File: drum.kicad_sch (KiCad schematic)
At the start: 39 parts, among them J101 CORTEX-DEBUG, J102 JAE_DX07S016JA3, SW101 SW_Push, SW102 SW_Push, U101 ATSAMD51J, U102 TPS78433QWDRBRQ1, Y101 32k768

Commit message: Update parts
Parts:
- C101: footprint Capacitor_SMD:C_0603_1608Metric -> V2_Capacitor_SMD:C_0603; symbol Device:C_Small -> V2_Device:C_0603_10u; Manufacturer (none) -> TDK; Mouser (none) -> 810-C1608X6S1A106M; Product (none) -> C1608X6S1A106M080AC
- C102, C103, C104, C105, C106: footprint Capacitor_SMD:C_0603_1608Metric -> V2_Capacitor_SMD:C_0603; symbol Device:C_Small -> V2_Device:C_0603_0u1; Manufacturer (none) -> TDK; Mouser (none) -> 810-CGA3E2X7R1H104MA; Product (none) -> CGA3E2X7R1H104M080AA
- C107, C108: footprint Capacitor_SMD:C_0603_1608Metric -> V2_Capacitor_SMD:C_0603; symbol Device:C_Small -> V2_Device:C_0603_18p; Manufacturer (none) -> YAGEO; Mouser (none) -> 603-CC603JRNPO9BN180; Product (none) -> CC0603JRNPO9BN180
- C109, C110: footprint Capacitor_SMD:C_0805_2012Metric -> V2_Capacitor_SMD:C_0805; symbol Device:C_Small -> V2_Device:C_0805_10u; Manufacturer (none) -> TDK; Mouser (none) -> 810-C2012X5R1E106K; Product (none) -> C2012X5R1E106K125AB; Rating (none) -> 25V
- D101: footprint LED_SMD:LED_0603_1608Metric -> V2_LED:LED_0603; symbol Device:LED_Small -> V2_Device:LED_0603_Orange; Manufacturer (none) -> ROHM Semiconductor; Mouser (none) -> 755-SML-D12M8WT86C; Product (none) -> SML-D12M8WT86C
- D102, D103: LCSC (none) -> C965555; Manufacturer (none) -> Worldsemi; Product (none) -> WS2812B-2020
- ESD101: Manufacturer (none) -> Semtech; Mouser (none) -> 947-RCLAMP0582N.TCT; Product (none) -> RCLAMP0582N.TCT
- FID101, FID102, FID103: value Fiducial -> Fiducial_Paste
- INFO102: value ORDER-NUMBER -> Order_Number
- J101: value CORTEX-DEBUG -> Cortex_Debug
- J102: value JAE_DX07S016JA3 -> DX07S016JA3; Manufacturer (none) -> JAE Electronics; Mouser (none) -> 656-DX07S016JA3R1500; Product (none) -> DX07S016JA3R1500
- R101: footprint Resistor_SMD:R_0603_1608Metric -> V2_Resistor_SMD:R_0603; symbol Device:R_Small -> V2_Device:R_0603_330R; Manufacturer (none) -> Vishay; Mouser (none) -> 71-CRCW0603330RFKEAC; Product (none) -> CRCW0603330RFKEAC; Rating (none) -> 100mW
- R102, R103: footprint Resistor_SMD:R_0603_1608Metric -> V2_Resistor_SMD:R_0603; symbol Device:R_Small -> V2_Device:R_0603_5k1; Manufacturer (none) -> Vishay; Mouser (none) -> 71-CRCW06035K10FKEAC; Product (none) -> CRCW06035K10FKEAC; Rating (none) -> 100mW
- R104: footprint Resistor_SMD:R_0603_1608Metric -> V2_Resistor_SMD:R_0603; symbol Device:R_Small -> V2_Device:R_0603_100k; Manufacturer (none) -> Vishay; Mouser (none) -> 71-CRCW0603100KFKEAC; Product (none) -> CRCW0603100KFKEAC; Rating (none) -> 100mW
- SW101, SW102: value SW_Push -> SKSG; symbol Switch:SW_Push -> V2_Switch:SKSG; Manufacturer (none) -> Alps Alpine; Mouser (none) -> 688-SKSGACE010; Product (none) -> SKSGACE010
- TVS101: value SMAJ36CA -> SMBJ36CA; footprint Diode_SMD:D_SMA -> V2_Diode_SMD:D_SMB; symbol V2_Diode:SMAJ36CA -> V2_Diode:SMBJ36CA; Manufacturer (none) -> Bourns; Mouser (none) -> 652-SMBJ36CA-Q; Product (none) -> SMBJ36CA-Q; Rating (none) -> 36V
- U101: Manufacturer (none) -> Microchip Technology; Mouser (none) -> 556-ATSAMD51J19AMU; Product (none) -> ATSAMD51J19A-MU
- U102: Manufacturer (none) -> Texas Instruments; Mouser (none) -> 595-TPS78433QWDRBRQ1; Product (none) -> TPS78433QWDRBRQ1
- Y101: symbol Device:Crystal_Small -> V2_Device:Crystal_3.2x1.5_32k768; Manufacturer (none) -> ABRACON; Mouser (none) -> 815-ABS0716632.768KT; Product (none) -> ABS07-166-32.768KHZ-T
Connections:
- net USB-Shield renamed Shield
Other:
- moved on the sheet: FID101, FID102, FID103, INFO102

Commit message: Update library
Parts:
- C101: Rating (none) -> 10V
- C102, C103, C104, C105, C106: Rating (none) -> 50V
- D101: Mouser 755-SML-D12M8WT86C -> 755-SML-D12D1WT86; Product SML-D12M8WT86C -> SML-D12D1WT86
- TVS101: value SMBJ36CA -> SMBJ33CA; symbol V2_Diode:SMBJ36CA -> V2_Diode:SMBJ33CA; Mouser 652-SMBJ36CA-Q -> 652-SMBJ33CA-Q; Product SMBJ36CA-Q -> SMBJ33CA-Q; Rating 36V -> 33V
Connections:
- net +24V-Supply renamed +VLINK
- net VBUS renamed +VBUS
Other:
- note added: "Power +28V"
- note removed: "Power +24V"
- moved on the sheet: TVS101

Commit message: Update library
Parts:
- J101: value Cortex_Debug -> Cortex; footprint V2_Cortex_Debug:Cortex_Debug_Pad -> V2_Connector_Debug:Cortex; symbol V2_Cortex_Debug:Cortex_Debug -> V2_Connector_Debug:Cortex
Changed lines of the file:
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@@
 		(at 240.03 170.18 0)
 		(unit 1)
-		(exclude_from_sim yes)
+		(exclude_from_sim no)
 		(in_bom no)
 		(on_board yes)
@@
 			)
 		)
+		(property "Sim.Enable" "0"
+			(at 240.03 170.18 0)
+			(effects
+				(font
+					(size 1.27 1.27)
+				)
+				(hide yes)
+			)
+		)
 		(instances
 			(project ""
@@
 		(at 227.33 180.34 0)
 		(unit 1)
-		(exclude_from_sim yes)
+		(exclude_from_sim no)
 		(in_bom no)
 		(on_board yes)
@@
 			)
 		)
+		(property "Sim.Enable" "0"
+			(at 227.33 180.34 0)
+			(effects
+				(font
+					(size 1.27 1.27)
+				)
+				(hide yes)
+			)
+		)
 		(instances
 			(project "pulse"
@@
 		(at 157.48 190.5 270)
 		(unit 1)
-		(exclude_from_sim yes)
+		(exclude_from_sim no)
 		(in_bom no)
 		(on_board yes)
@@
 			)
 		)
+		(property "Sim.Enable" "0"
+			(at 157.48 190.5 0)
+			(effects
+				(font
+					(size 1.27 1.27)
+				)
+				(hide yes)
+			)
+		)
 		(instances
 			(project "hihat-1"
@@
 	)
 	(symbol
-		(lib_id "V2_Cortex_Debug:Cortex_Debug")
+		(lib_id "V2_Connector_Debug:Cortex")
 		(at 124.46 107.95 0)
 		(unit 1)
@@
 			)
 		)
-		(property "Value" "Cortex_Debug"
+		(property "Value" "Cortex"
 			(at 125.73 97.79 0)
 			(effects
@@
 			)
 		)
-		(property "Footprint" "V2_Cortex_Debug:Cortex_Debug_Pad"
+		(property "Footprint" "V2_Connector_Debug:Cortex"
 			(at 124.46 121.92 0)
 			(effects
@@
 		(at 240.03 165.1 0)
 		(unit 1)
-		(exclude_from_sim yes)
+		(exclude_from_sim no)
 		(in_bom no)
 		(on_board yes)
@@
 			)
 		)
+		(property "Sim.Enable" "0"
+			(at 240.03 165.1 0)
+			(effects
+				(font
+					(size 1.27 1.27)
+				)
+				(hide yes)
+			)
+		)
 		(instances
 			(project ""
@@
 		(at 157.48 184.15 270)
 		(unit 1)
-		(exclude_from_sim yes)
+		(exclude_from_sim no)
 		(in_bom no)
 		(on_board yes)
@@
 			)
 		)
+		(property "Sim.Enable" "0"
+			(at 157.48 184.15 0)
+			(effects
+				(font
+					(size 1.27 1.27)
+				)
+				(hide yes)
+			)
+		)
 		(instances
 			(project "hihat-1"
@@
 		(at 157.48 177.8 270)
 		(unit 1)
-		(exclude_from_sim yes)
+		(exclude_from_sim no)
 		(in_bom no)
 		(on_board yes)
@@
 			)
 		)
+		(property "Sim.Enable" "0"
+			(at 157.48 177.8 0)
+			(effects
+				(font
+					(size 1.27 1.27)
+				)
+				(hide yes)
+			)
+		)
 		(instances
 			(project "hihat-1"
@@
 		(at 157.48 171.45 270)
 		(unit 1)
-		(exclude_from_sim yes)
+		(exclude_from_sim no)
 		(in_bom no)
 		(on_board yes)
@@
 			)
 		)
+		(property "Sim.Enable" "0"
+			(at 157.48 171.45 0)
+			(effects
+				(font
+					(size 1.27 1.27)
+				)
+				(hide yes)
+			)
+		)
 		(instances
 			(project ""
@@
 		(at 212.09 167.64 0)
 		(unit 1)
-		(exclude_from_sim yes)
+		(exclude_from_sim no)
 		(in_bom no)
 		(on_board yes)
@@
 			(at 212.09 167.64 0)
 			(effects
+				(font
+					(size 1.27 1.27)
+				)
+				(hide yes)
+			)
+		)
+		(property "Sim.Enable" "0"
+			(at 212.09 167.64 0)
+			(effects

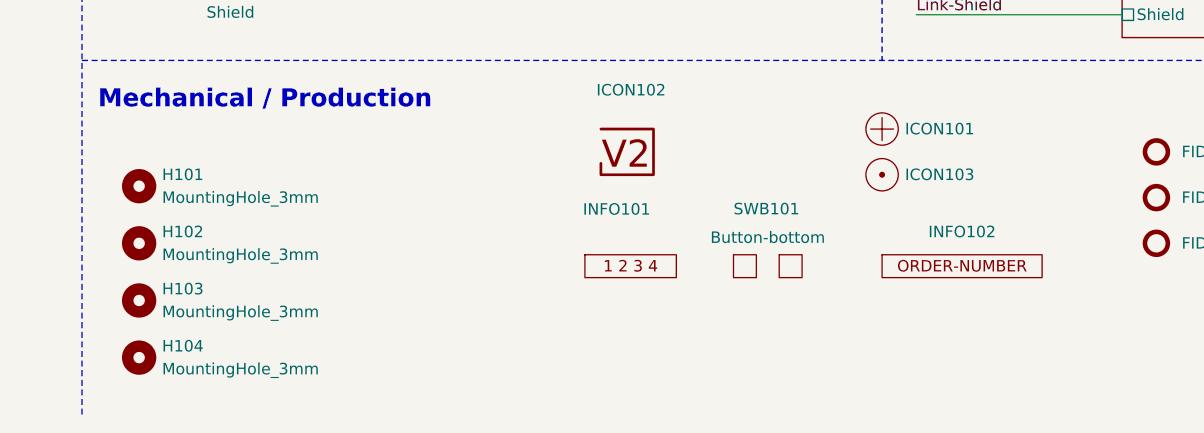
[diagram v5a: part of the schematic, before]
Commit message: Replace Order_Number
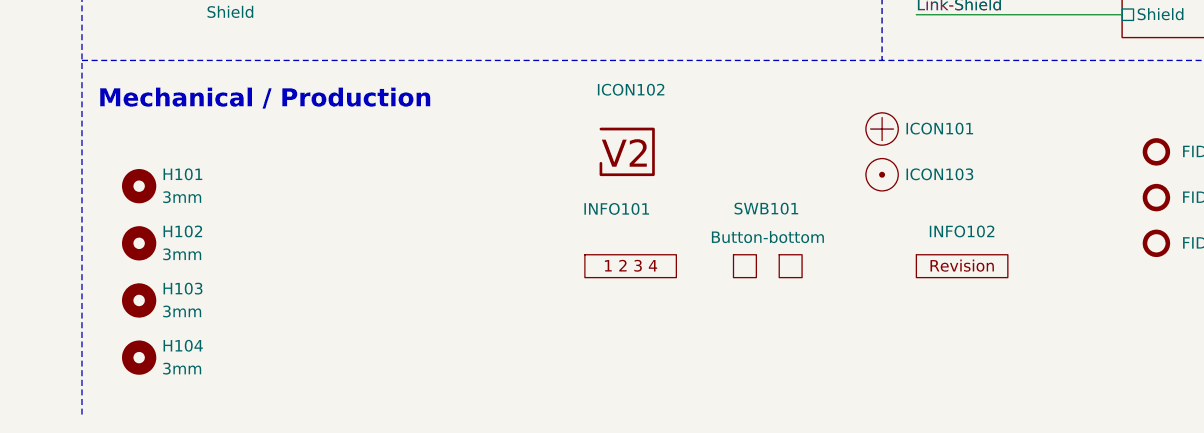
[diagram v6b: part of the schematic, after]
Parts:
- H101, H102, H103, H104: value MountingHole_3mm -> 3mm
- INFO102: value Order_Number -> (none); footprint V2_Production:Order_Number -> V2_Production:Revision; symbol V2_Production:Order_Number -> V2_Production:Revision
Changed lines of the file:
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@@
 			)
 		)
-		(property "Value" "MountingHole_3mm"
+		(property "Value" "3mm"
 			(at 160.02 191.7699 90)
 			(effects
@@
 			)
 		)
-		(property "Sim.Enable" "0"
-			(at 157.48 190.5 0)
-			(effects
-				(font
-					(size 1.27 1.27)
-				)
-				(hide yes)
-			)
-		)
 		(instances
 			(project "hihat-1"
@@
 	)
 	(symbol
-		(lib_id "V2_Production:Order_Number")
+		(lib_id "V2_Production:Revision")
 		(at 248.92 180.34 0)
 		(unit 1)
@@
 			)
 		)
-		(property "Value" "Order_Number"
+		(property "Value" ""
 			(at 248.92 182.88 0)
 			(effects
@@
 			)
 		)
-		(property "Footprint" "V2_Production:Order_Number"
+		(property "Footprint" "V2_Production:Revision"
 			(at 248.92 185.42 0)
 			(effects
@@
 			)
 		)
-		(property "Value" "MountingHole_3mm"
+		(property "Value" "3mm"
 			(at 160.02 185.4199 90)
 			(effects
@@
 			)
 		)
-		(property "Sim.Enable" "0"
-			(at 157.48 184.15 0)
-			(effects
-				(font
-					(size 1.27 1.27)
-				)
-				(hide yes)
-			)
-		)
 		(instances
 			(project "hihat-1"
@@
 			)
 		)
-		(property "Value" "MountingHole_3mm"
+		(property "Value" "3mm"
 			(at 160.02 179.0699 90)
 			(effects
@@
 			)
 		)
-		(property "Sim.Enable" "0"
-			(at 157.48 177.8 0)
-			(effects
-				(font
-					(size 1.27 1.27)
-				)
-				(hide yes)
-			)
-		)
 		(instances
 			(project "hihat-1"
@@
 			)
 		)
-		(property "Value" "MountingHole_3mm"
+		(property "Value" "3mm"
 			(at 160.02 172.7199 90)
 			(effects
@@
 			)
 		)
-		(property "Sim.Enable" "0"
-			(at 157.48 171.45 0)
-			(effects
-				(font
-					(size 1.27 1.27)
-				)
-				(hide yes)
-			)
-		)
 		(instances
 			(project ""
@@
 			(at 212.09 167.64 0)
 			(effects
-				(font
-					(size 1.27 1.27)
-				)
-				(hide yes)
-			)
-		)
-		(property "Sim.Enable" "0"
-			(at 212.09 167.64 0)
-			(effects

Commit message: Update Library
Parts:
- C101: symbol V2_Device:C_0603_10u -> V2_Capacitor:0603_10u
- C102, C103, C104, C105, C106: symbol V2_Device:C_0603_0u1 -> V2_Capacitor:0603_0u1
- C107, C108: symbol V2_Device:C_0603_18p -> V2_Capacitor:0603_18p
- C109, C110: symbol V2_Device:C_0805_10u -> V2_Capacitor:0805_10u
- D101: symbol V2_Device:LED_0603_Orange -> V2_LED:0603_Orange
- INFO102: value (none) -> ~
- R101: symbol V2_Device:R_0603_330R -> V2_Resistor:0603_330R
- R102, R103: symbol V2_Device:R_0603_5k1 -> V2_Resistor:0603_5k1
- R104: symbol V2_Device:R_0603_100k -> V2_Resistor:0603_100k
- Y101: symbol V2_Device:Crystal_3.2x1.5_32k768 -> V2_Crystal:3.2x1.5_32k768
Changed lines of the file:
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@@
 	)
 	(symbol
-		(lib_id "V2_Device:C_0603_0u1")
+		(lib_id "V2_Capacitor:0603_0u1")
 		(at 109.22 24.13 0)
 		(unit 1)
@@
 		(at 240.03 170.18 0)
 		(unit 1)
-		(exclude_from_sim no)
+		(exclude_from_sim yes)
 		(in_bom no)
 		(on_board yes)
@@
 	)
 	(symbol
-		(lib_id "V2_Device:LED_0603_Orange")
+		(lib_id "V2_LED:0603_Orange")
 		(at 129.54 86.36 0)
 		(mirror y)
@@
 	)
 	(symbol
-		(lib_id "V2_Device:R_0603_5k1")
+		(lib_id "V2_Resistor:0603_5k1")
 		(at 203.2 119.38 90)
 		(unit 1)
@@
 		(at 227.33 180.34 0)
 		(unit 1)
-		(exclude_from_sim no)
+		(exclude_from_sim yes)
 		(in_bom no)
 		(on_board yes)
@@
 	)
 	(symbol
-		(lib_id "V2_Device:C_0805_10u")
+		(lib_id "V2_Capacitor:0805_10u")
 		(at 55.88 180.34 0)
 		(unit 1)
@@
 	)
 	(symbol
-		(lib_id "V2_Device:C_0603_0u1")
+		(lib_id "V2_Capacitor:0603_0u1")
 		(at 119.38 24.13 0)
 		(unit 1)
@@
 		(at 240.03 165.1 0)
 		(unit 1)
-		(exclude_from_sim no)
+		(exclude_from_sim yes)
 		(in_bom no)
 		(on_board yes)
@@
 			)
 		)
-		(property "Value" ""
+		(property "Value" "~"
 			(at 248.92 182.88 0)
 			(effects
@@
 	)
 	(symbol
-		(lib_id "V2_Device:C_0805_10u")
+		(lib_id "V2_Capacitor:0805_10u")
 		(at 30.48 180.34 0)
 		(unit 1)
@@
 	)
 	(symbol
-		(lib_id "V2_Device:Crystal_3.2x1.5_32k768")
+		(lib_id "V2_Crystal:3.2x1.5_32k768")
 		(at 24.13 43.18 0)
 		(unit 1)
@@
 	)
 	(symbol
-		(lib_id "V2_Device:C_0603_18p")
+		(lib_id "V2_Capacitor:0603_18p")
 		(at 26.67 46.99 0)
 		(unit 1)
@@
 	)
 	(symbol
-		(lib_id "V2_Device:C_0603_10u")
+		(lib_id "V2_Capacitor:0603_10u")
 		(at 57.15 24.13 0)
 		(unit 1)
@@
 	)
 	(symbol
-		(lib_id "V2_Device:C_0603_18p")
+		(lib_id "V2_Capacitor:0603_18p")
 		(at 21.59 46.99 0)
 		(unit 1)
@@
 	)
 	(symbol
-		(lib_id "V2_Device:R_0603_330R")
+		(lib_id "V2_Resistor:0603_330R")
 		(at 138.43 86.36 90)
 		(unit 1)
@@
 	)
 	(symbol
-		(lib_id "V2_Device:C_0603_0u1")
+		(lib_id "V2_Capacitor:0603_0u1")
 		(at 99.06 24.13 0)
 		(unit 1)
@@
 	)
 	(symbol
-		(lib_id "V2_Device:C_0603_0u1")
+		(lib_id "V2_Capacitor:0603_0u1")
 		(at 78.74 24.13 0)
 		(unit 1)
@@
 	)
 	(symbol
-		(lib_id "V2_Device:R_0603_5k1")
+		(lib_id "V2_Resistor:0603_5k1")
 		(at 203.2 116.84 90)
 		(unit 1)
@@
 	)
 	(symbol
-		(lib_id "V2_Device:C_0603_0u1")
+		(lib_id "V2_Capacitor:0603_0u1")
 		(at 88.9 24.13 0)
 		(unit 1)
@@
 	)
 	(symbol
-		(lib_id "V2_Device:R_0603_100k")
+		(lib_id "V2_Resistor:0603_100k")
 		(at 50.8 121.92 90)
 		(unit 1)

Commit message: Refresh
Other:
- moved on the sheet: TVS101
